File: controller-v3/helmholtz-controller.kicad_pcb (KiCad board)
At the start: 2 copper layers, 72.7 x 72.1 mm, 57 parts, among them J1 Screw_Terminal_01x02, J2 Screw_Terminal_01x02, J3 Screw_Terminal_01x02, J4 Screw_Terminal_01x02, J5 Conn_01x04, U1 DRV8871DDA, U2 DRV8871DDA, U3 INA226, U4 INA226, U5 DRV8871DDA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

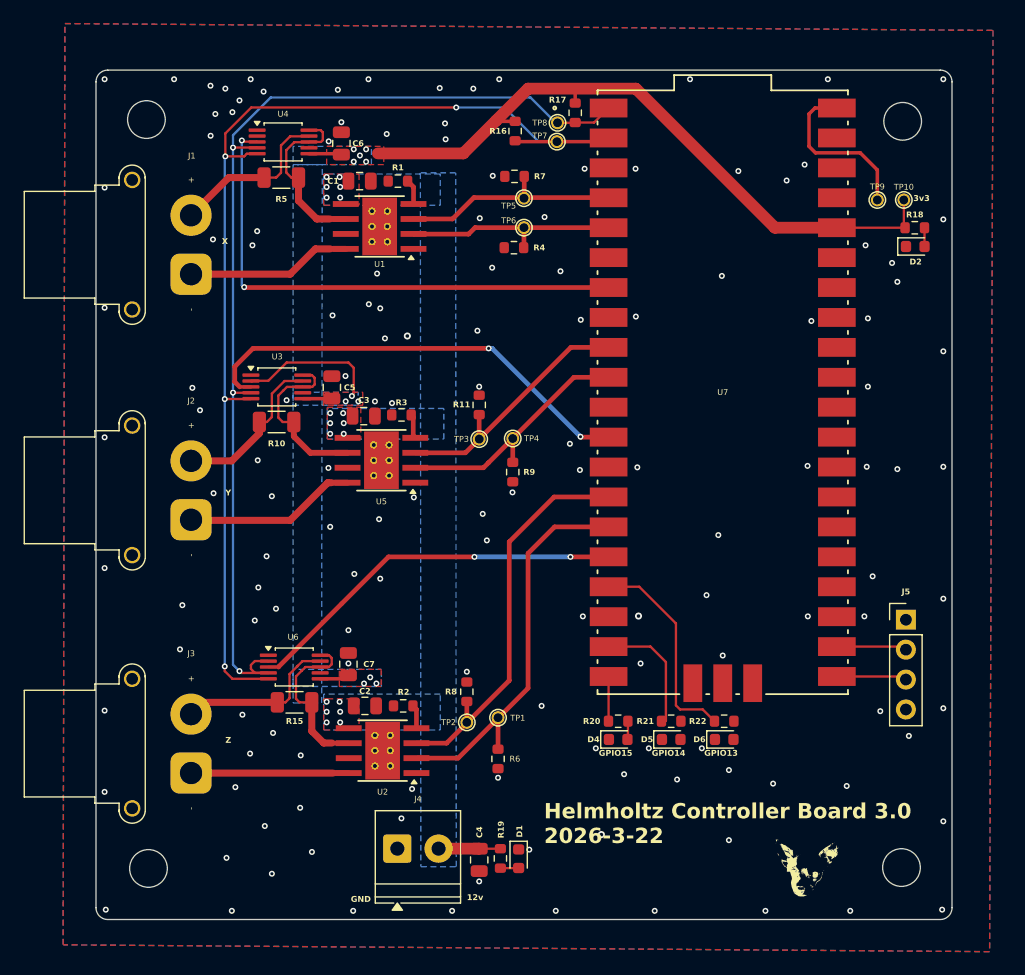
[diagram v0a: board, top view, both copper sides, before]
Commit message: Helholtz cage controller v3.0, upgrade to KICad 10, new gitignore file
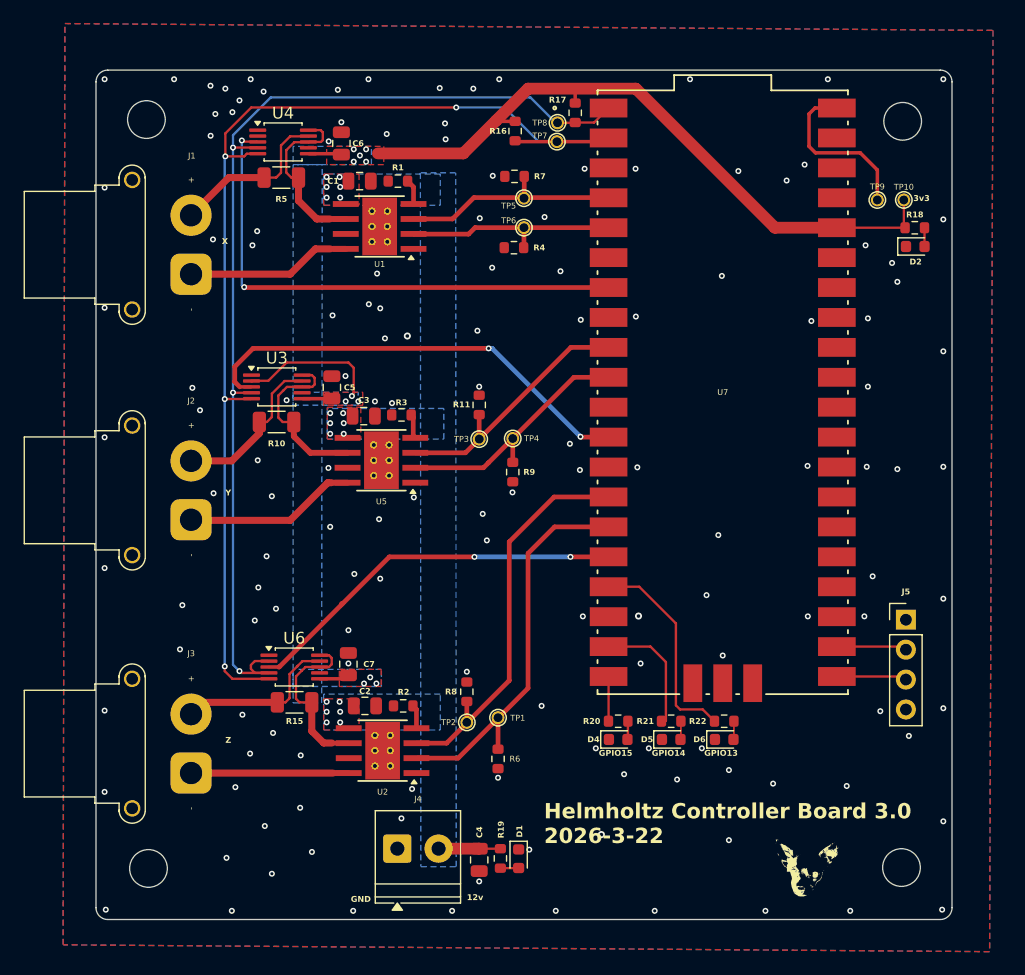
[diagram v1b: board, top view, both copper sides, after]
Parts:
- J1, J2, J3: value Screw_Terminal_01x02 -> XT30 PCB-mount
- J4: value Screw_Terminal_01x02 -> 1751248
- J5: value Conn_01x04 -> 0022112042
- R2: value 32K -> 32k
- U3, U4, U6: footprint Package_SO:VSSOP-10_3x3mm_P0.5mm -> Package_SO:TSSOP-10_3x3mm_P0.5mm
- U7: value RPi_Pico -> SC0915
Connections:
- net /D4 renamed Net-(U7-GPIO15)
- net /D5 renamed Net-(U7-GPIO14)
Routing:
- net Net-(D6-A): track 0.00 -> 1.57 mm
- net Net-(D5-A): track 0.00 -> 1.57 mm
